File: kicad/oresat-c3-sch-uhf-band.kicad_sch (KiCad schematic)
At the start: 125 parts, among them Q3 NTR4101, Q4 PMV45EN, U16 AX5043, U18 LT5534, U19 BDCN-20-13+, U20 QPC1022, U21 TQP7M9105, U22 LT5534, U25 SN74LVC1G11IDCKRQ1, U26 TLV7041DBV, U27 LP2985AIM5-1.8_NOPB, U29 TQP3M9036, U32 SF2446E, U33 SF2446E, U40 MAX941EUA+, X1 TYKTBLSANF-16.000000

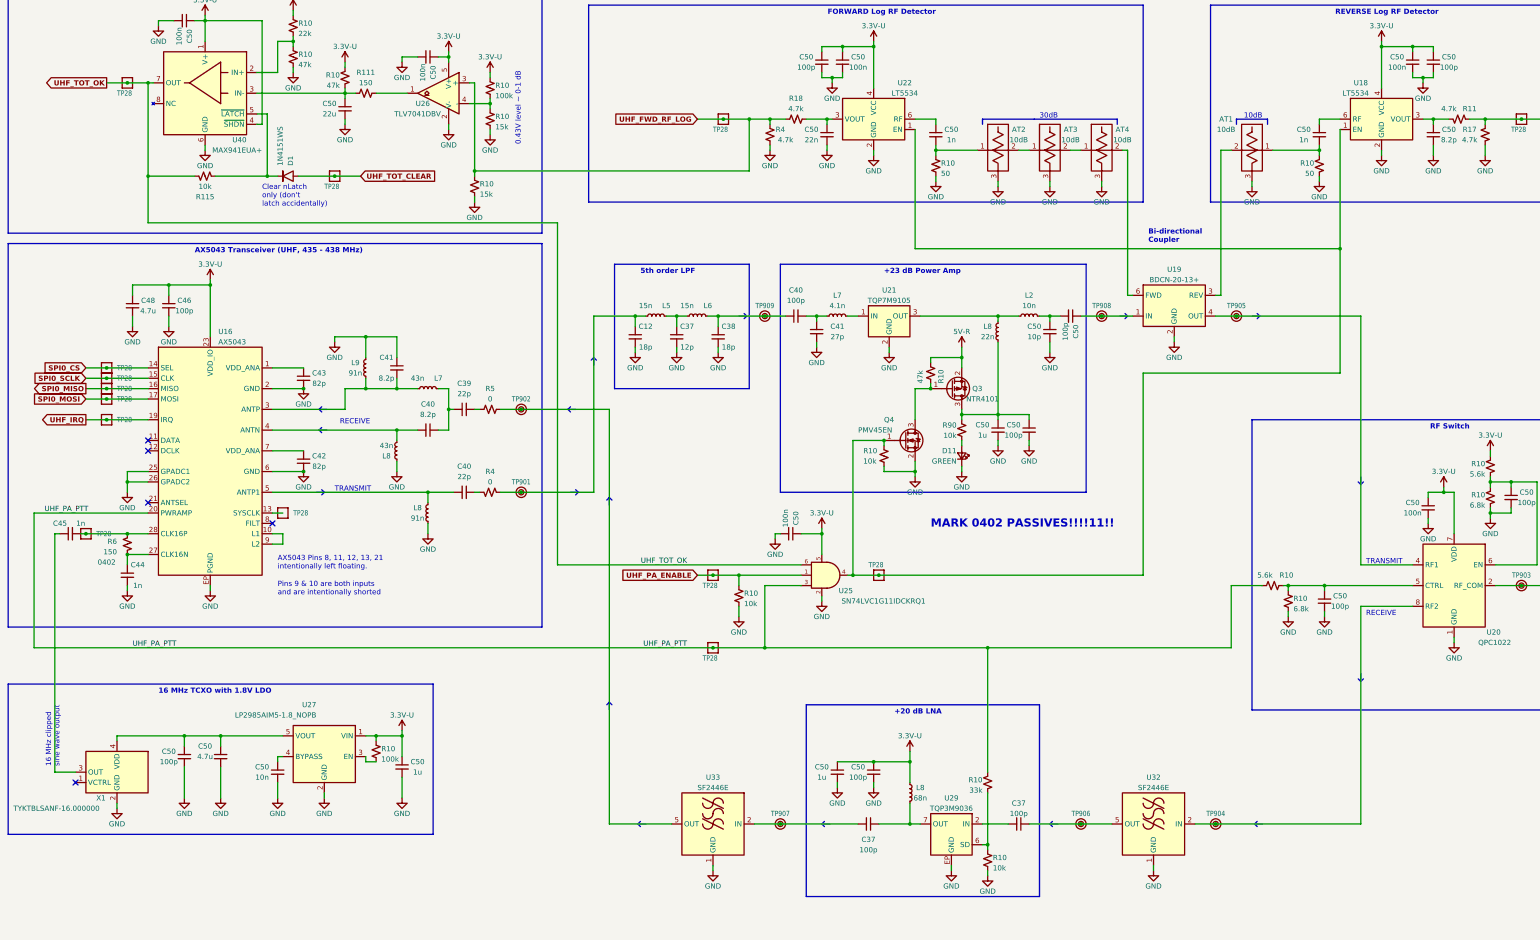
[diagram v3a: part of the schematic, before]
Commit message: Cleaned up RF routing. Stitched (automatically). RF routing cleanup. Marked 0402s and replacedsome 0603 with 0402. Silkscreen cleanup. Just BOM optimization and purchasing left.
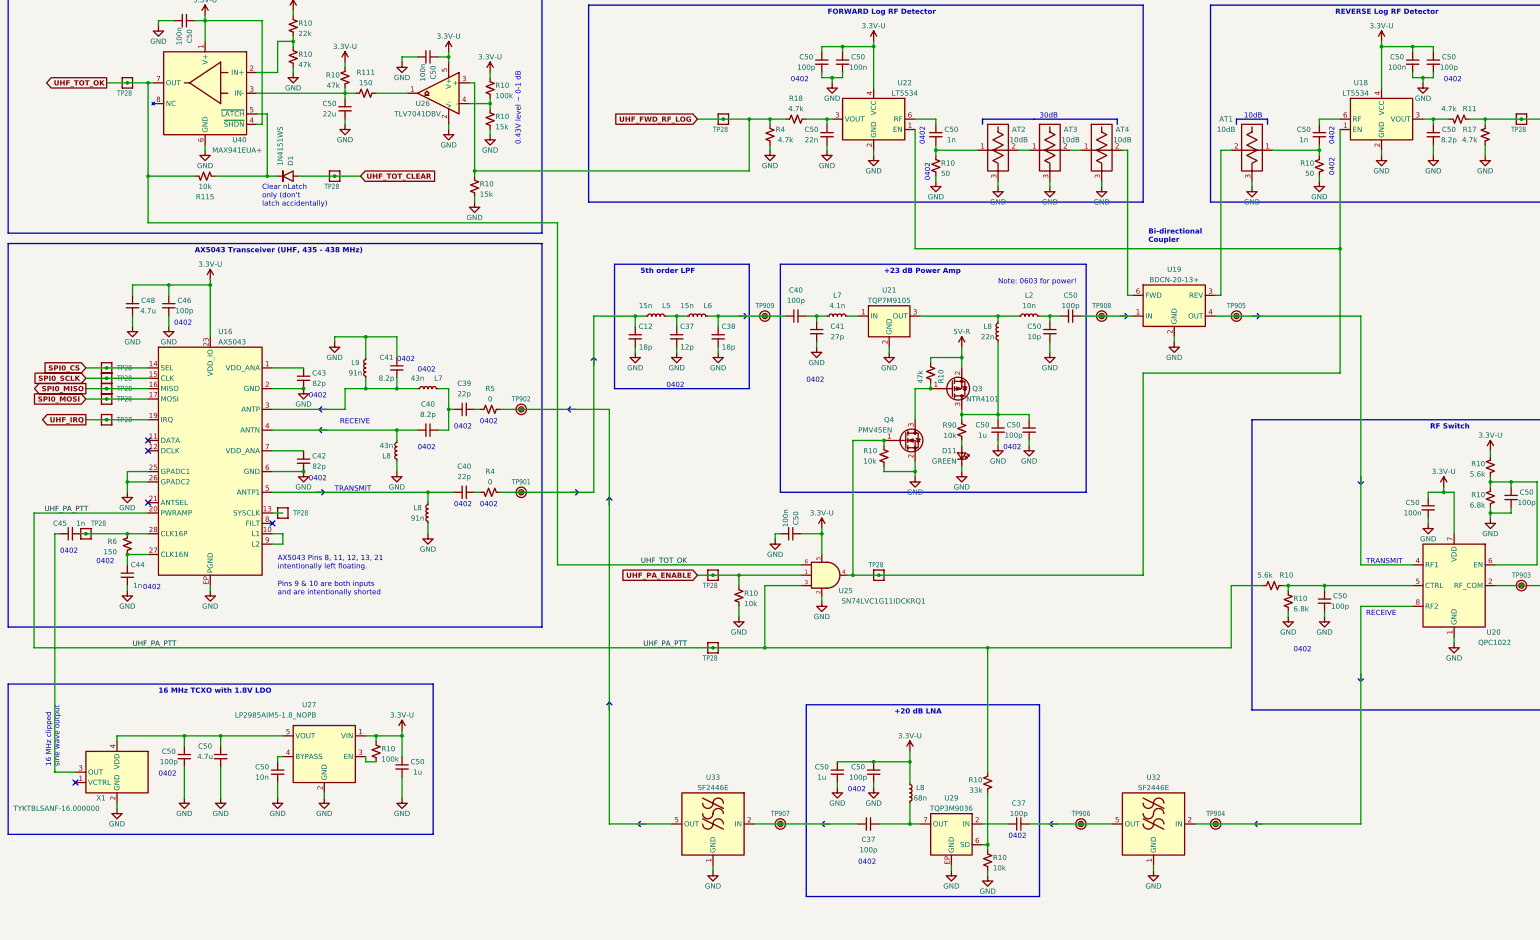
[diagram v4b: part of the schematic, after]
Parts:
- C46, C50: footprint Capacitor_SMD:C_0603_1608Metric -> Capacitor_SMD:C_0402_1005Metric
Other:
- note added: "0402"
- note added: "Note: 0603 for power!"
- note removed: "MARK 0402 PASSIVES!!!!11!!"
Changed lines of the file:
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@@
     (effects (font (size 1.27 1.27) (thickness 0.254) bold) (justify left bottom))
   )
+  (text "0402" (at 114.3 134.62 0)
+    (effects (font (size 1.27 1.27)) (justify left bottom))
+  )
   (text "Pins 9 & 10 are both inputs\nand are intentionally shorted"
     (at 80.01 170.18 0)
@@
     (effects (font (size 1.27 1.27)) (justify left bottom))
   )
-  (text "MARK 0402 PASSIVES!!!!11!!" (at 240.03 153.67 0)
-    (effects (font (size 2 2) (thickness 0.4) bold (color 255 0 0 1)) (justify left bottom))
+  (text "0402" (at 219.71 218.44 0)
+    (effects (font (size 1.27 1.27)) (justify left bottom))
+  )
+  (text "0402" (at 222.25 236.22 0)
+    (effects (font (size 1.27 1.27)) (justify left bottom))
   )
   (text "+20 dB LNA" (at 231.14 199.39 0)
     (effects (font (size 1.27 1.27) (thickness 0.254) bold) (justify left bottom))
   )
+  (text "0402" (at 328.93 184.15 0)
+    (effects (font (size 1.27 1.27)) (justify left bottom))
+  )
   (text "Clear nLatch\nonly (don't\nlatch accidentally)" (at 76.2 74.93 0)
     (effects (font (size 1.27 1.27)) (justify left bottom))
@@
     (effects (font (size 1.27 1.27)) (justify left bottom))
   )
+  (text "0402" (at 123.19 148.59 0)
+    (effects (font (size 1.27 1.27)) (justify left bottom))
+  )
   (text "Tx Time Out Timer (TOT)" (at 90.17 17.78 0)
     (effects (font (size 1.27 1.27) (thickness 0.254) bold) (justify right bottom))
   )
+  (text "0402" (at 109.22 113.03 0)
+    (effects (font (size 1.27 1.27)) (justify left bottom))
+  )
   (text "REVERSE Log RF Detector" (at 364.49 27.94 0)
     (effects (font (size 1.27 1.27) (thickness 0.254) bold) (justify right bottom))
   )
+  (text "0402" (at 54.61 104.14 0)
+    (effects (font (size 1.27 1.27)) (justify left bottom))
+  )
+  (text "0402" (at 50.8 214.63 0)
+    (effects (font (size 1.27 1.27)) (justify left bottom))
+  )
   (text "TRANSMIT" (at 346.71 162.56 0)
     (effects (font (size 1.27 1.27)) (justify left bottom))
@@
     (effects (font (size 1.27 1.27)) (justify left bottom))
   )
+  (text "0402" (at 87.63 121.92 0)
+    (effects (font (size 1.27 1.27)) (justify left bottom))
+  )
   (text "5th order LPF" (at 168.91 91.44 0)
     (effects (font (size 1.27 1.27) (thickness 0.254) bold) (justify left bottom))
   )
+  (text "0402" (at 46.99 168.91 0)
+    (effects (font (size 1.27 1.27)) (justify left bottom))
+  )
+  (text "0402" (at 339.09 59.69 90)
+    (effects (font (size 1.27 1.27)) (justify left bottom))
+  )
+  (text "0402" (at 26.67 160.02 0)
+    (effects (font (size 1.27 1.27)) (justify left bottom))
+  )
+  (text "0402" (at 35.56 162.56 0)
+    (effects (font (size 1.27 1.27)) (justify left bottom))
+  )
   (text "10dB" (at 321.31 53.34 0)
     (effects (font (size 1.27 1.27)) (justify right bottom))
   )
+  (text "Note: 0603 for power!" (at 256.54 93.98 0)
+    (effects (font (size 1.27 1.27)) (justify left bottom))
+  )
+  (text "0402" (at 365.76 44.45 0)
+    (effects (font (size 1.27 1.27)) (justify left bottom))
+  )
   (text "16 MHz clipped \nsine wave output\n" (at 26.67 212.09 90)
     (effects (font (size 1.27 1.27)) (justify left bottom))
   )
+  (text "0402" (at 205.74 44.45 0)
+    (effects (font (size 1.27 1.27)) (justify left bottom))
+  )
   (text "AX5043 Pins 8, 11, 12, 13, 21\nintentionally left floating."
     (at 80.01 163.83 0)
     (effects (font (size 1.27 1.27)) (justify left bottom))
   )
+  (text "0402" (at 87.63 142.24 0)
+    (effects (font (size 1.27 1.27)) (justify left bottom))
+  )
+  (text "0402" (at 257.81 134.62 0)
+    (effects (font (size 1.27 1.27)) (justify left bottom))
+  )
+  (text "0402" (at 114.3 115.57 0)
+    (effects (font (size 1.27 1.27)) (justify left bottom))
+  )
+  (text "0402" (at 238.76 59.69 90)
+    (effects (font (size 1.27 1.27)) (justify left bottom))
+  )
   (text "+23 dB Power Amp" (at 228.6 91.44 0)
     (effects (font (size 1.27 1.27) (thickness 0.254) bold) (justify left bottom))
@@
     (effects (font (size 1.27 1.27)) (justify left bottom))
   )
+  (text "0402" (at 129.54 128.27 0)
+    (effects (font (size 1.27 1.27)) (justify left bottom))
+  )
   (text "16 MHz TCXO with 1.8V LDO" (at 50.8 194.31 0)
     (effects (font (size 1.27 1.27) (thickness 0.254) bold) (justify left bottom))
   )
+  (text "0402" (at 129.54 148.59 0)
+    (effects (font (size 1.27 1.27)) (justify left bottom))
+  )
+  (text "0402" (at 339.09 67.31 90)
+    (effects (font (size 1.27 1.27)) (justify left bottom))
+  )
   (text "TRANSMIT" (at 93.98 144.78 0)
     (effects (font (size 1.27 1.27)) (justify left bottom))
@@
     (effects (font (size 1.27 1.27) (thickness 0.254) bold) (justify left bottom))
   )
+  (text "0402" (at 240.03 68.58 90)
+    (effects (font (size 1.27 1.27)) (justify left bottom))
+  )
+  (text "0402" (at 209.55 118.11 0)
+    (effects (font (size 1.27 1.27)) (justify left bottom))
+  )
   (text "RF Switch" (at 372.11 129.54 0)
     (effects (font (size 1.27 1.27) (thickness 0.254) bold) (justify right bottom))
@@
     (effects (font (size 1.27 1.27)) (justify left bottom))
   )
+  (text "0402" (at 175.26 119.38 0)
+    (effects (font (size 1.27 1.27)) (justify left bottom))
+  )
+  (text "0402" (at 259.08 229.87 0)
+    (effects (font (size 1.27 1.27)) (justify left bottom))
+  )
   (text "FORWARD Log RF Detector" (at 241.3 27.94 0)
     (effects (font (size 1.27 1.27) (thickness 0.254) bold) (justify right bottom))
   )
+  (text "0402" (at 123.19 129.54 0)
+    (effects (font (size 1.27 1.27)) (justify left bottom))
+  )
   (label "UHF_PA_PTT" (at 44.45 182.88 0) (fields_autoplaced)
     (effects (font (size 1.27 1.27)) (justify left bottom))
@@
       (effects (font (size 1.27 1.27)))
     )
-    (property "Footprint" "Capacitor_SMD:C_0603_1608Metric" (at 363.22 39.37 0)
+    (property "Footprint" "Capacitor_SMD:C_0402_1005Metric" (at 363.22 39.37 0)
       (effects (font (size 1.27 1.27)) hide)
     )
@@
   )
   (symbol (lib_id "oresat-misc:Test-Point-1mm-round") (at 33.02 154.94 0) (unit 1)
-    (in_bom yes) (on_board yes) (dnp no) (fields_autoplaced)
-    (property "Reference" "TP28" (at 35.56 154.94 0)
+    (in_bom yes) (on_board yes) (dnp no)
+    (property "Reference" "TP28" (at 34.29 152.4 0)
       (effects (font (size 1.27 1.0795)) (justify left))
     )
@@
       (effects (font (size 1.27 1.27)))
     )
-    (property "Footprint" "Capacitor_SMD:C_0603_1608Metric" (at 53.34 99.06 0)
+    (property "Footprint" "Capacitor_SMD:C_0402_1005Metric" (at 53.34 99.06 0)
       (effects (font (size 1.27 1.27)) hide)
     )
@@
       (effects (font (size 1.27 1.27)))
     )
-    (property "Footprint" "Capacitor_SMD:C_0603_1608Metric" (at 57.15 209.55 0)
+    (property "Footprint" "Capacitor_SMD:C_0402_1005Metric" (at 57.15 209.55 0)
       (effects (font (size 1.27 1.27)) hide)
     )
@@
       (effects (font (size 1.27 1.27)))
     )
-    (property "Footprint" "Capacitor_SMD:C_0603_1608Metric" (at 264.16 129.54 0)
+    (property "Footprint" "Capacitor_SMD:C_0402_1005Metric" (at 264.16 129.54 0)
       (effects (font (size 1.27 1.27)) hide)
     )
@@
     )
     (property "Package" "0402" (at 38.1 161.925 0)
-      (effects (font (size 1.27 1.27)))
+      (effects (font (size 1.27 1.27)) hide)
     )
     (pin "1")
@@
   (symbol (lib_id "Device:C_Small") (at 274.32 101.6 270) (unit 1)
     (in_bom yes) (on_board yes) (dnp no)
-    (property "Reference" "C50" (at 275.59 105.41 0)
+    (property "Reference" "C50" (at 274.32 96.52 90)
       (effects (font (size 1.27 1.27)))
     )
-    (property "Value" "100p" (at 273.05 105.41 0)
+    (property "Value" "100p" (at 274.32 99.06 90)
       (effects (font (size 1.27 1.27)))
     )
@@
       (effects (font (size 1.27 1.27)))
     )
-    (property "Footprint" "Capacitor_SMD:C_0603_1608Metric" (at 213.36 39.37 0)
+    (property "Footprint" "Capacitor_SMD:C_0402_1005Metric" (at 213.36 39.37 0)
       (effects (font (size 1.27 1.27)) hide)
     )
@@
       (effects (font (size 1.27 1.27)))
     )
-    (property "Footprint" "Capacitor_SMD:C_0603_1608Metric" (at 226.06 213.36 0)
+    (property "Footprint" "Capacitor_SMD:C_0402_1005Metric" (at 226.06 213.36 0)
       (effects (font (size 1.27 1.27)) hide)
     )

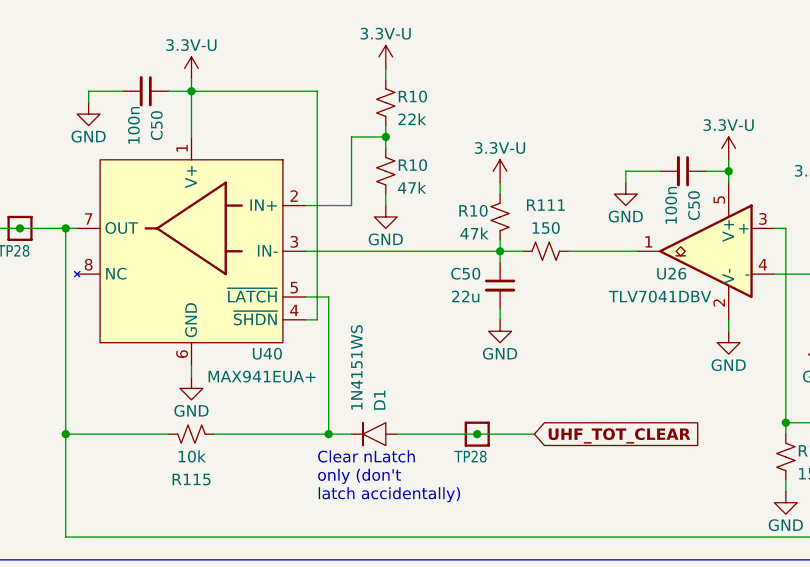
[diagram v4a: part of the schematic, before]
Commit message: Cleanup of crystals, more BOM reduction and fixes.
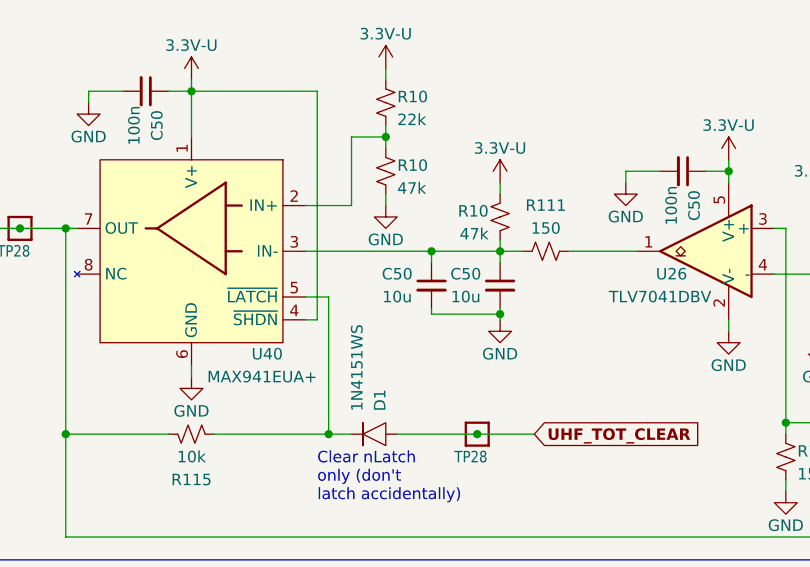
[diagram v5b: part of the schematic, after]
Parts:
- added C50: 10u, Capacitor_SMD:C_0603_1608Metric, symbol Device:C_Small
- C50: value 22u -> 10u
- R10: footprint Resistor_SMD:R_0402_1005Metric -> Resistor_SMD:R_0603_1608Metric
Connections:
- net GND: now also C50.2
- net at C50.1, R10.2, R111.1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: now also C50.1
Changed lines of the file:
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@@
   (junction (at 104.14 204.47) (diameter 0) (color 0 0 0 0)
   )
+  (junction (at 96.52 53.975) (diameter 0) (color 0 0 0 0)
+  )
   (junction (at 86.36 119.38) (diameter 0) (color 0 0 0 0)
   )
@@
   (junction (at 121.92 38.1) (diameter 0) (color 0 0 0 0)
   )
+  (junction (at 88.9 46.99) (diameter 0) (color 0 0 0 0)
+  )
   (junction (at 256.54 101.6) (diameter 0) (color 0 0 0 0)
   )
@@
     (stroke (width 0) (type default))
   )
+  (wire (pts (xy 88.9 46.99) (xy 74.93 46.99))
+    (stroke (width 0) (type default))
+  )
   (wire (pts (xy 77.47 67.31) (xy 77.47 52.07))
     (stroke (width 0) (type default))
@@
     (stroke (width 0) (type default))
   )
+  (wire (pts (xy 88.9 53.975) (xy 96.52 53.975))
+    (stroke (width 0) (type default))
+  )
   (wire (pts (xy 48.26 44.45) (xy 43.18 44.45))
     (stroke (width 0) (type default))
@@
     (stroke (width 0) (type default))
   )
+  (wire (pts (xy 88.9 53.34) (xy 88.9 53.975))
+    (stroke (width 0) (type default))
+  )
   (polyline (pts (xy 345.44 142.875) (xy 345.44 140.97))
     (stroke (width 0.254) (type default) (color 146 146 146 1))
@@
     (stroke (width 0) (type default))
   )
-  (wire (pts (xy 96.52 46.99) (xy 74.93 46.99))
+  (wire (pts (xy 96.52 46.99) (xy 88.9 46.99))
     (stroke (width 0) (type default))
   )
@@
     (stroke (width 0) (type default))
   )
-  (wire (pts (xy 96.52 53.34) (xy 96.52 54.61))
+  (wire (pts (xy 96.52 53.34) (xy 96.52 53.975))
     (stroke (width 0) (type default))
   )
@@
     (stroke (width 0) (type default))
   )
+  (wire (pts (xy 96.52 53.975) (xy 96.52 54.61))
+    (stroke (width 0) (type default))
+  )
   (polyline (pts (xy 90.17 129.54) (xy 90.805 130.175))
     (stroke (width 0.254) (type default) (color 146 146 146 1))
@@
     (stroke (width 0) (type default))
   )
+  (wire (pts (xy 88.9 46.99) (xy 88.9 48.26))
+    (stroke (width 0) (type default))
+  )
   (wire (pts (xy 215.9 43.18) (xy 213.36 43.18))
     (stroke (width 0) (type default))
@@
     )
   )
+  (symbol (lib_id "Device:C_Small") (at 88.9 50.8 0) (mirror y) (unit 1)
+    (in_bom yes) (on_board yes) (dnp no)
+    (property "Reference" "C50" (at 85.09 49.53 0)
+      (effects (font (size 1.27 1.27)))
+    )
+    (property "Value" "10u" (at 85.09 52.07 0)
+      (effects (font (size 1.27 1.27)))
+    )
+    (property "Footprint" "Capacitor_SMD:C_0603_1608Metric" (at 88.9 50.8 0)
+      (effects (font (size 1.27 1.27)) hide)
+    )
+    (property "Datasheet" "~" (at 88.9 50.8 0)
+      (effects (font (size 1.27 1.27)) hide)
+    )
+    (pin "1")
+    (pin "2")
+    (instances
+      (project "oresat-c3"
+        (path "/65d12cdd-c326-4033-9053-c59fa4e0b25e/1b68ea4b-cacf-4529-b1d4-9be5d7c1043c"
+          (reference "C50") (unit 1)
+        )
+        (path "/65d12cdd-c326-4033-9053-c59fa4e0b25e/05e45903-5042-4bc1-87af-e9d7510ea02d"
+          (reference "C61") (unit 1)
+        )
+      )
+    )
+  )
   (symbol (lib_id "power:GND") (at 43.18 168.91 0) (mirror y) (unit 1)
     (in_bom yes) (on_board yes) (dnp no)
@@
       (effects (font (size 1.27 1.27)))
     )
-    (property "Value" "22u" (at 92.71 52.07 0)
+    (property "Value" "10u" (at 92.71 52.07 0)
       (effects (font (size 1.27 1.27)))
     )
@@
       (effects (font (size 1.27 1.27)) (justify left))
     )
-    (property "Footprint" "Resistor_SMD:R_0402_1005Metric" (at 128.27 69.85 0)
+    (property "Footprint" "Resistor_SMD:R_0603_1608Metric" (at 128.27 69.85 0)
       (effects (font (size 1.27 1.27)) hide)
     )
